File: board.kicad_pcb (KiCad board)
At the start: 2 copper layers, 82.6 x 54.4 mm, 34 parts, among them J1 Conn_02x16_Odd_Even, J2 JSTBATT, Q1 2N7002, SW1 SW_SPDT, U1 BQ24075RGT, U2 nRF52840_holyiot_18010, U3 XC6206PxxxMR, U4 SRV05-4

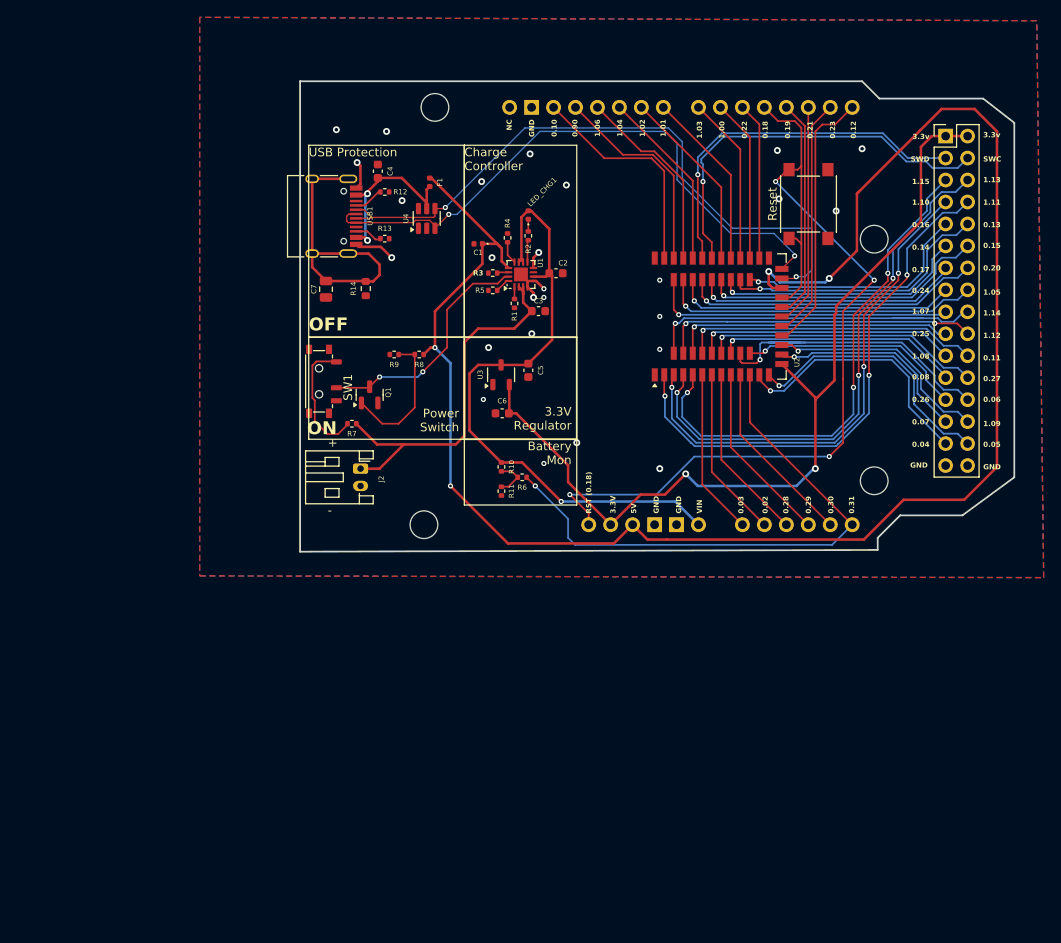
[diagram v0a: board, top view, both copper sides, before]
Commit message: Updated to revision 0.2, with Holyiot module on edge of board
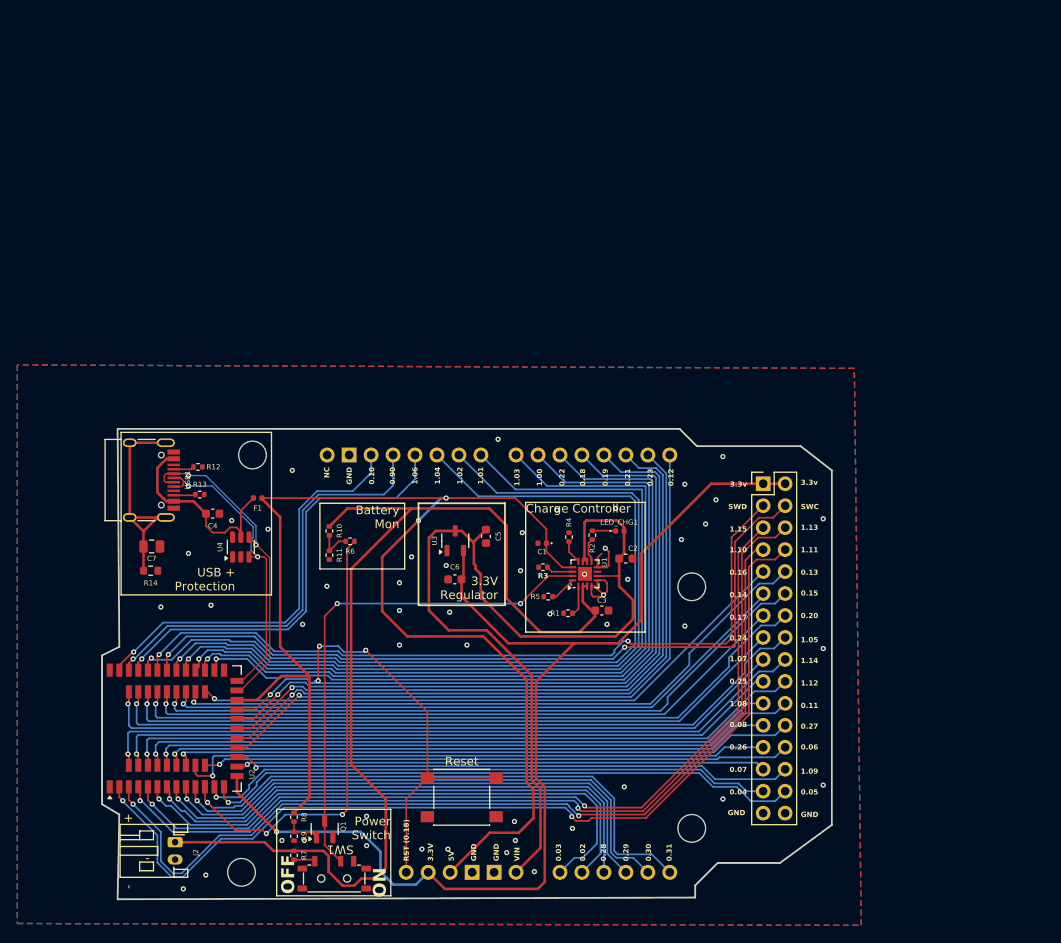
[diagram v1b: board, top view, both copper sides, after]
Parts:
- moved SW_Reset1 79.5 mm to (141.7, 119.6), turned to 180 degrees
- moved U2 79.0 mm to (106.7, 111.7)
- moved SW1 57.5 mm to (127.0, 129.0), turned to 180 degrees
- moved R9 56.9 mm to (122.3, 124.1), turned to -90 degrees
- moved R8 55.4 mm to (122.3, 121.9), turned to -90 degrees
- moved Q1 50.5 mm to (125.8, 123.3)
- moved R7 50.4 mm to (122.3, 126.3), turned to -90 degrees
- moved J2 48.2 mm to (108.5, 124.8)
- moved J1 45.4 mm to (176.6, 83.3)
- moved A1 45.4 mm to (102.3, 130.8)
- moved C4 44.0 mm to (112.9, 86.8), turned to 180 degrees
- moved U4 43.7 mm to (116.2, 90.7)
- moved F1 41.6 mm to (118.1, 85.0), turned to 180 degrees
- moved R14 41.0 mm to (105.7, 93.4), turned to 180 degrees
- moved R12 38.4 mm to (111.2, 81.4)
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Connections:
- J1 pad 19: /P0.25 -> /P1.12
- J1 pad 20: /P1.12 -> /P0.25
- J1 pad 21: /P1.08 -> /P0.11
- J1 pad 22: /P0.11 -> /P1.08
- J1 pad 23: /P0.08 -> /P0.27
- J1 pad 24: /P0.27 -> /P0.08
- J1 pad 25: /P0.26 -> /P0.06
- J1 pad 26: /P0.06 -> /P0.26
- R10 pad 1: +VSW -> +BATT
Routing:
- net /P1.04: track 20.9 -> 102.2 mm, vias 0 -> 1
- net +BATT: track 44.4 -> 122.5 mm
- net /P1.02: track 21.3 -> 97.1 mm, vias 0 -> 1
- net /P1.01: track 20.7 -> 95.1 mm, vias 0 -> 1
- net /P1.03: track 19.4 -> 91.0 mm, vias 0 -> 1
- net /P1.00: track 18.8 -> 88.4 mm, vias 0 -> 1
- net /P0.22: track 18.2 -> 85.7 mm, vias 0 -> 1
- net /P0.19: track 25.6 -> 80.4 mm, vias 0 -> 1
- net /P0.21: track 25.8 -> 79.2 mm, vias 0 -> 1
- net /P0.23: track 28.0 -> 78.1 mm, vias 0 -> 1
- net /P0.31: track 65.4 -> 115.4 mm, vias 1 -> 3
- net /P1.11: track 61.6 -> 111.0 mm, vias 3 -> 2
- net /P1.10: track 58.3 -> 107.4 mm, vias 3 -> 2
- net +5V: track 202.2 -> 154.7 mm, vias 4 -> 2
- net /P0.12: track 31.0 -> 78.0 mm, vias 0 -> 1
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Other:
- board size 82.6 x 54.4 mm -> 84.4 x 54.4 mm
- board text added: "USB + Protection"
- board text removed: "USB Protection"

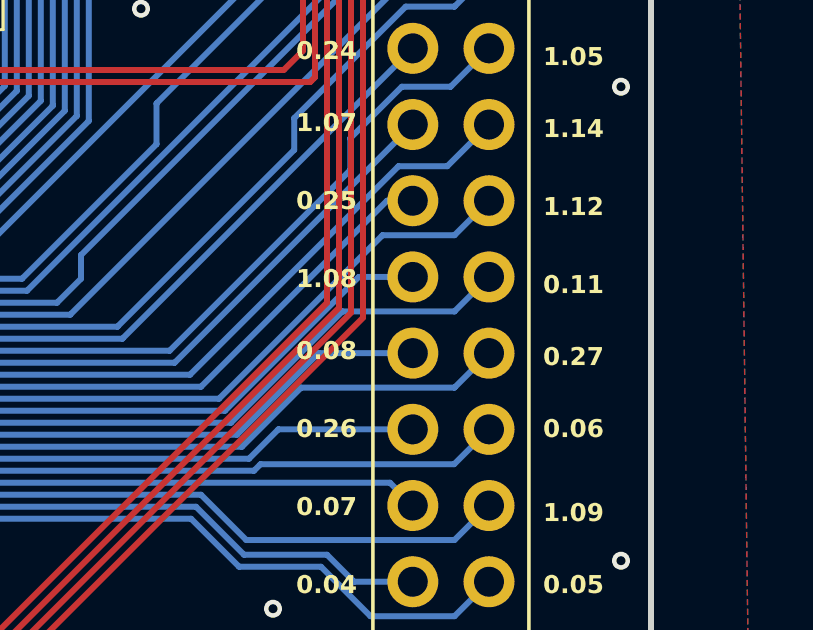
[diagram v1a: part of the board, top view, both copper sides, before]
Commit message: Updated silkscreen
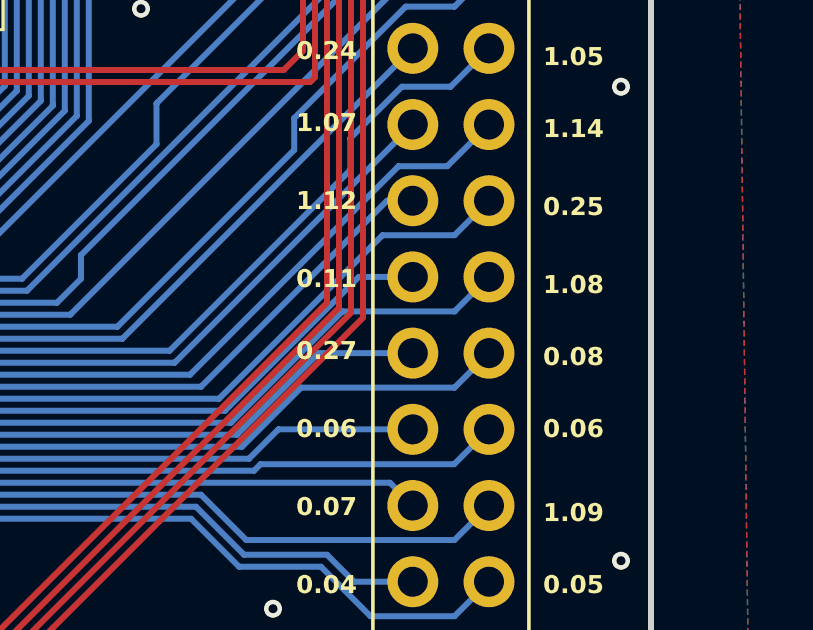
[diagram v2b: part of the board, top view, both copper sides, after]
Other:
- board text removed: "0.26"
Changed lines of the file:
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@@
 		(tags "fuse")
 		(property "Reference" "F1"
-			(at 0 -1.17 360)
+			(at 0 -1.17 0)
 			(layer "F.SilkS")
 			(effects
@@
 		)
 		(property "Value" "500mA"
-			(at 0 1.17 360)
+			(at 0 1.17 0)
 			(layer "F.Fab")
 			(effects
@@
 		)
 		(fp_text user "${REFERENCE}"
-			(at 0 0 360)
+			(at 0 0 0)
 			(layer "F.Fab")
 			(effects
@@
 		(tags "resistor")
 		(property "Reference" "R1"
-			(at 1.49 0 360)
+			(at 1.49 0 0)
 			(layer "F.SilkS")
 			(effects
@@
 		)
 		(property "Value" "10k"
-			(at 0 1.17 360)
+			(at 0 1.17 0)
 			(layer "F.Fab")
 			(effects
@@
 		)
 		(fp_text user "${REFERENCE}"
-			(at 0 0 360)
+			(at 0 0 0)
 			(layer "F.Fab")
 			(effects
@@
 		(tags "tact sw push 6mm smd")
 		(property "Reference" "SW_Reset1"
-			(at 0 -4.05 360)
+			(at 0 -4.05 0)
 			(layer "F.SilkS")
 			(hide yes)
@@
 		)
 		(property "Value" "Reset"
-			(at 0 4.15 360)
+			(at 0 4.15 0)
 			(layer "F.SilkS")
 			(effects
@@
 		)
 		(fp_text user "${REFERENCE}"
-			(at 0 -4.05 360)
+			(at 0 -4.05 0)
 			(layer "F.Fab")
 			(effects
@@
 		)
 	)
-	(gr_text "1.08"
+	(gr_text "0.11"
 		(at 174.7 108.8 0)
 		(layer "F.SilkS")
@@
 		)
 	)
-	(gr_text "0.26"
+	(gr_text "0.06"
 		(at 174.7 113.8 0)
 		(layer "F.SilkS")
@@
 		)
 	)
-	(gr_text "0.11"
+	(gr_text "1.08"
 		(at 180.9 109 0)
 		(layer "F.SilkS")
@@
 		)
 	)
-	(gr_text "0.27"
+	(gr_text "0.08"
 		(at 180.9 111.4 0)
 		(layer "F.SilkS")
@@
 		)
 	)
-	(gr_text "1.12"
+	(gr_text "0.25"
 		(at 180.9 106.4 0)
 		(layer "F.SilkS")
@@
 		)
 	)
-	(gr_text "0.25"
+	(gr_text "1.12"
 		(at 174.7 106.2 0)
 		(layer "F.SilkS")
@@
 		)
 	)
-	(gr_text "0.08"
+	(gr_text "0.27"
 		(at 174.7 111.2 0)
 		(layer "F.SilkS")

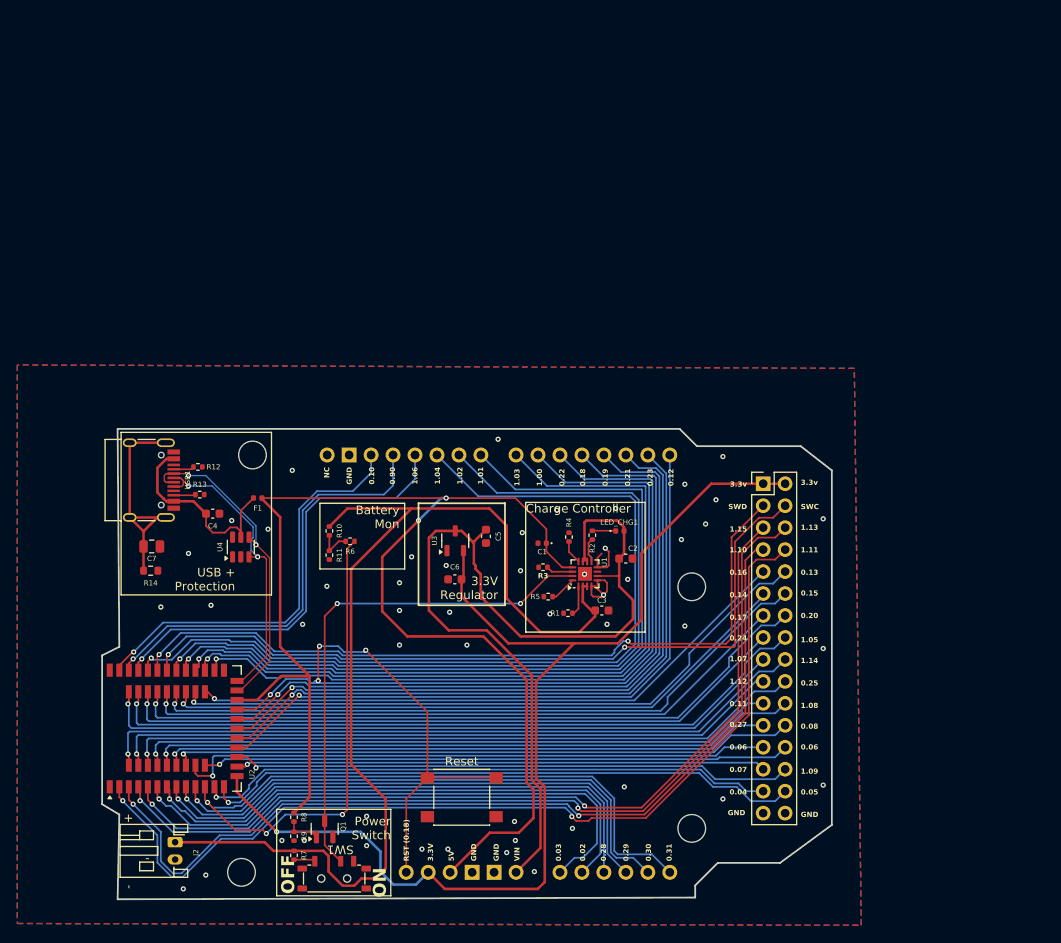
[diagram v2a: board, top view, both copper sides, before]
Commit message: Added debug / programming pins
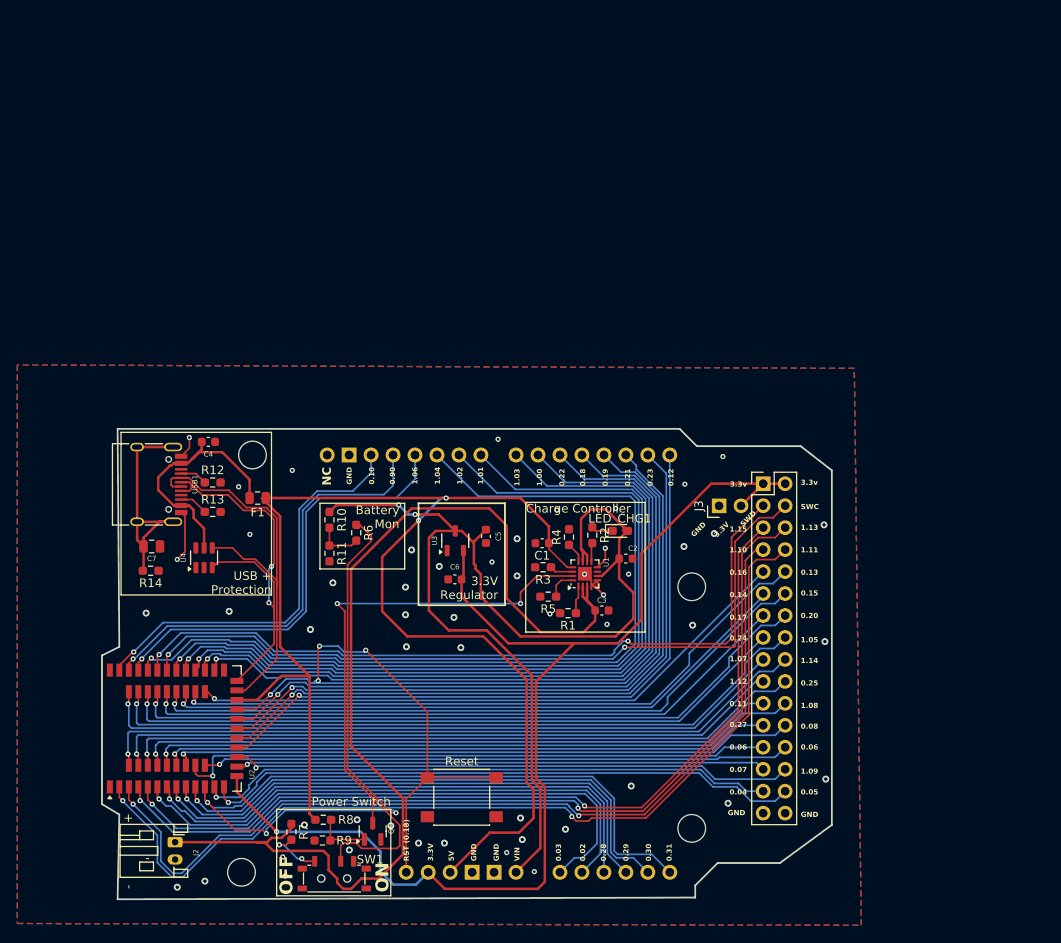
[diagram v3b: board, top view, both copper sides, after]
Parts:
- added J3: Conn_01x02_Socket, Connector_PinHeader_2.54mm:PinHeader_1x02_P2.54mm_Vertical, F.Cu at (171.5, 85.9)
- C1: footprint LED_SMD:LED_0402_1005Metric -> Capacitor_SMD:C_0603_1608Metric
- F1: footprint Fuse:Fuse_0402_1005Metric -> Fuse:Fuse_0805_2012Metric
- LED_CHG1: footprint LED_SMD:LED_0402_1005Metric -> LED_SMD:LED_0603_1608Metric_Pad1.05x0.95mm_HandSolder
- R1, R10, R11, R12, R13, R2, R3, R4, R5, R6, R7, R8, R9: footprint Resistor_SMD:R_0402_1005Metric -> Resistor_SMD:R_0603_1608Metric_Pad0.98x0.95mm_HandSolder
- R14: footprint Resistor_SMD:R_0603_1608Metric -> Resistor_SMD:R_0603_1608Metric_Pad0.98x0.95mm_HandSolder
- moved C4 8.32 mm to (112.4, 78.5)
- moved Q1 5.56 mm to (131.4, 123.5)
- moved U4 4.43 mm to (111.9, 91.9)
- moved R8 3.40 mm to (125.7, 122.2), turned to 0 degrees
- moved R9 3.32 mm to (125.6, 124.6), turned to 180 degrees
- moved R7 2.73 mm to (122.0, 123.6)
- moved R13 2.49 mm to (112.9, 86.6)
- moved R12 2.48 mm to (112.9, 83.2)
- moved R10 1.29 mm to (126.4, 87.5)
- moved R6 1.22 mm to (129.5, 89.0), turned to -90 degrees
- moved USB1 0.99 mm to (105.2, 83.4)
- moved R11 0.20 mm to (126.4, 91.4)
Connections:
- R10 pad 1: +BATT -> +VSW
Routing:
- net +VSW: track 107.1 -> 127.6 mm, vias 0 -> 2
- net SYSOFF: track 59.7 -> 72.7 mm
- net /P0.31: track 115.4 -> 128.0 mm
- net /D+: track 34.7 -> 47.2 mm
- net /D-: track 37.3 -> 48.1 mm, vias 2 -> 0
- net VBUS: track 23.8 -> 29.0 mm
- net Net-(SW1-A): track 2.22 -> 6.53 mm, vias 0 -> 2
- net GND: track 13.7 -> 17.6 mm, vias 50 -> 53
- net +3.3V: track 131.7 -> 135.3 mm
- net Net-(Q1-G): track 4.03 -> 6.30 mm
- net /P0.19: track 80.4 -> 79.0 mm
- net /P0.18: track 129.5 -> 128.2 mm
- net VSENSE: track 4.12 -> 5.40 mm
- net /P0.21: track 79.2 -> 78.0 mm
- net /P0.22: track 85.7 -> 84.6 mm
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
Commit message: Updated readme.  Fixed silkscreen
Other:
- board text added: "0.26"

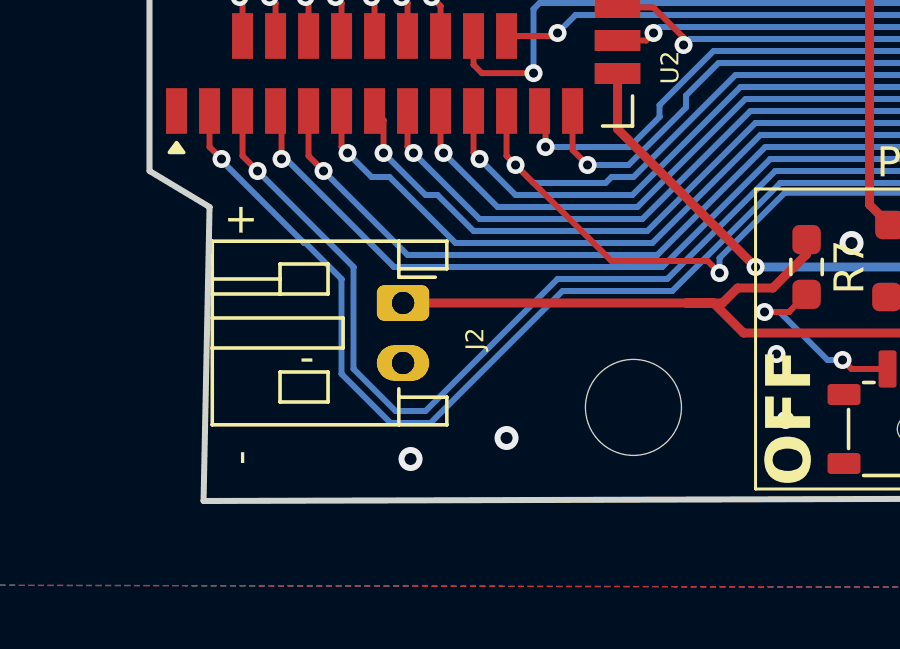
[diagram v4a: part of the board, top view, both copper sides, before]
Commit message: Fixed polarity of connector
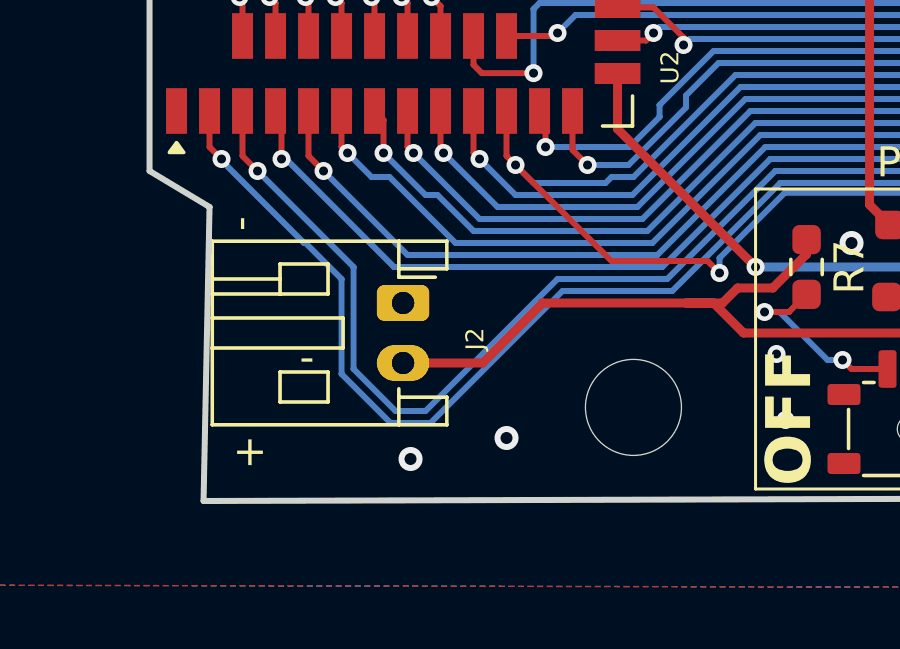
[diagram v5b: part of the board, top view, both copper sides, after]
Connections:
- J2 pad 1: +BATT -> GND
- J2 pad 2: GND -> +BATT
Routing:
- net +BATT: track 122.7 -> 123.6 mm
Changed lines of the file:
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@@
 			(size 0.85 0.85)
 			(drill 0.85)
-			(layers "*.Cu" "*.Mask")
+			(layers "*.Cu" "*.Mask" "In1.Cu" "In2.Cu" "In3.Cu" "In4.Cu" "In5.Cu" "In6.Cu"
+				"In7.Cu" "In8.Cu" "In9.Cu" "In10.Cu" "In11.Cu" "In12.Cu" "In13.Cu" "In14.Cu"
+				"In15.Cu" "In16.Cu" "In17.Cu" "In18.Cu" "In19.Cu" "In20.Cu" "In21.Cu"
+				"In22.Cu" "In23.Cu" "In24.Cu" "In25.Cu" "In26.Cu" "In27.Cu" "In28.Cu"
+				"In29.Cu" "In30.Cu"
+			)
 		)
 		(pad "" np_thru_hole circle
@@
 			(size 0.85 0.85)
 			(drill 0.85)
-			(layers "*.Cu" "*.Mask")
+			(layers "*.Cu" "*.Mask" "In1.Cu" "In2.Cu" "In3.Cu" "In4.Cu" "In5.Cu" "In6.Cu"
+				"In7.Cu" "In8.Cu" "In9.Cu" "In10.Cu" "In11.Cu" "In12.Cu" "In13.Cu" "In14.Cu"
+				"In15.Cu" "In16.Cu" "In17.Cu" "In18.Cu" "In19.Cu" "In20.Cu" "In21.Cu"
+				"In22.Cu" "In23.Cu" "In24.Cu" "In25.Cu" "In26.Cu" "In27.Cu" "In28.Cu"
+				"In29.Cu" "In30.Cu"
+			)
 		)
 		(pad "1" smd roundrect
@@
 			(remove_unused_layers no)
 			(roundrect_rratio 0.208333)
-			(net 57 "+BATT")
+			(net 23 "GND")
 			(pinfunction "Pin_1")
 			(pintype "passive")
@@
 			)
 			(remove_unused_layers no)
-			(net 23 "GND")
+			(net 57 "+BATT")
 			(pinfunction "Pin_2")
 			(pintype "passive")
@@
 	)
 	(gr_text "-"
-		(at 103.7 130.2 90)
+		(at 103.7 122.4 90)
 		(layer "F.SilkS")
 		(effects
@@
 	)
 	(gr_text "+"
-		(at 103.7 122.6 90)
+		(at 104 130.35 90)
 		(layer "F.SilkS")
 		(effects
@@
 	)
 	(segment
+		(start 111.2 126.8)
+		(end 108.55 126.8)
+		(width 0.3)
+		(layer "F.Cu")
+		(net 57)
+	)
+	(segment
 		(start 157.125 97.825)
 		(end 155.9 96.6)
@@
 	)
 	(segment
+		(start 118 124.8)
+		(end 113.2 124.8)
+		(width 0.3)
+		(layer "F.Cu")
+		(net 57)
+	)
+	(segment
 		(start 156.2 96.9)
 		(end 156.2 95.2)
@@
 	)
 	(segment
-		(start 118 124.8)
-		(end 108.55 124.8)
+		(start 113.2 124.8)
+		(end 111.2 126.8)
 		(width 0.3)
 		(layer "F.Cu")
